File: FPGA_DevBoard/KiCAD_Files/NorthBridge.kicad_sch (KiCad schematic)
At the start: 11 parts, among them J1 4677, J2 DM3D-SF, U1 W25Q128JVSIQ TR, U14 ESP32-WROOM-32UE-N8

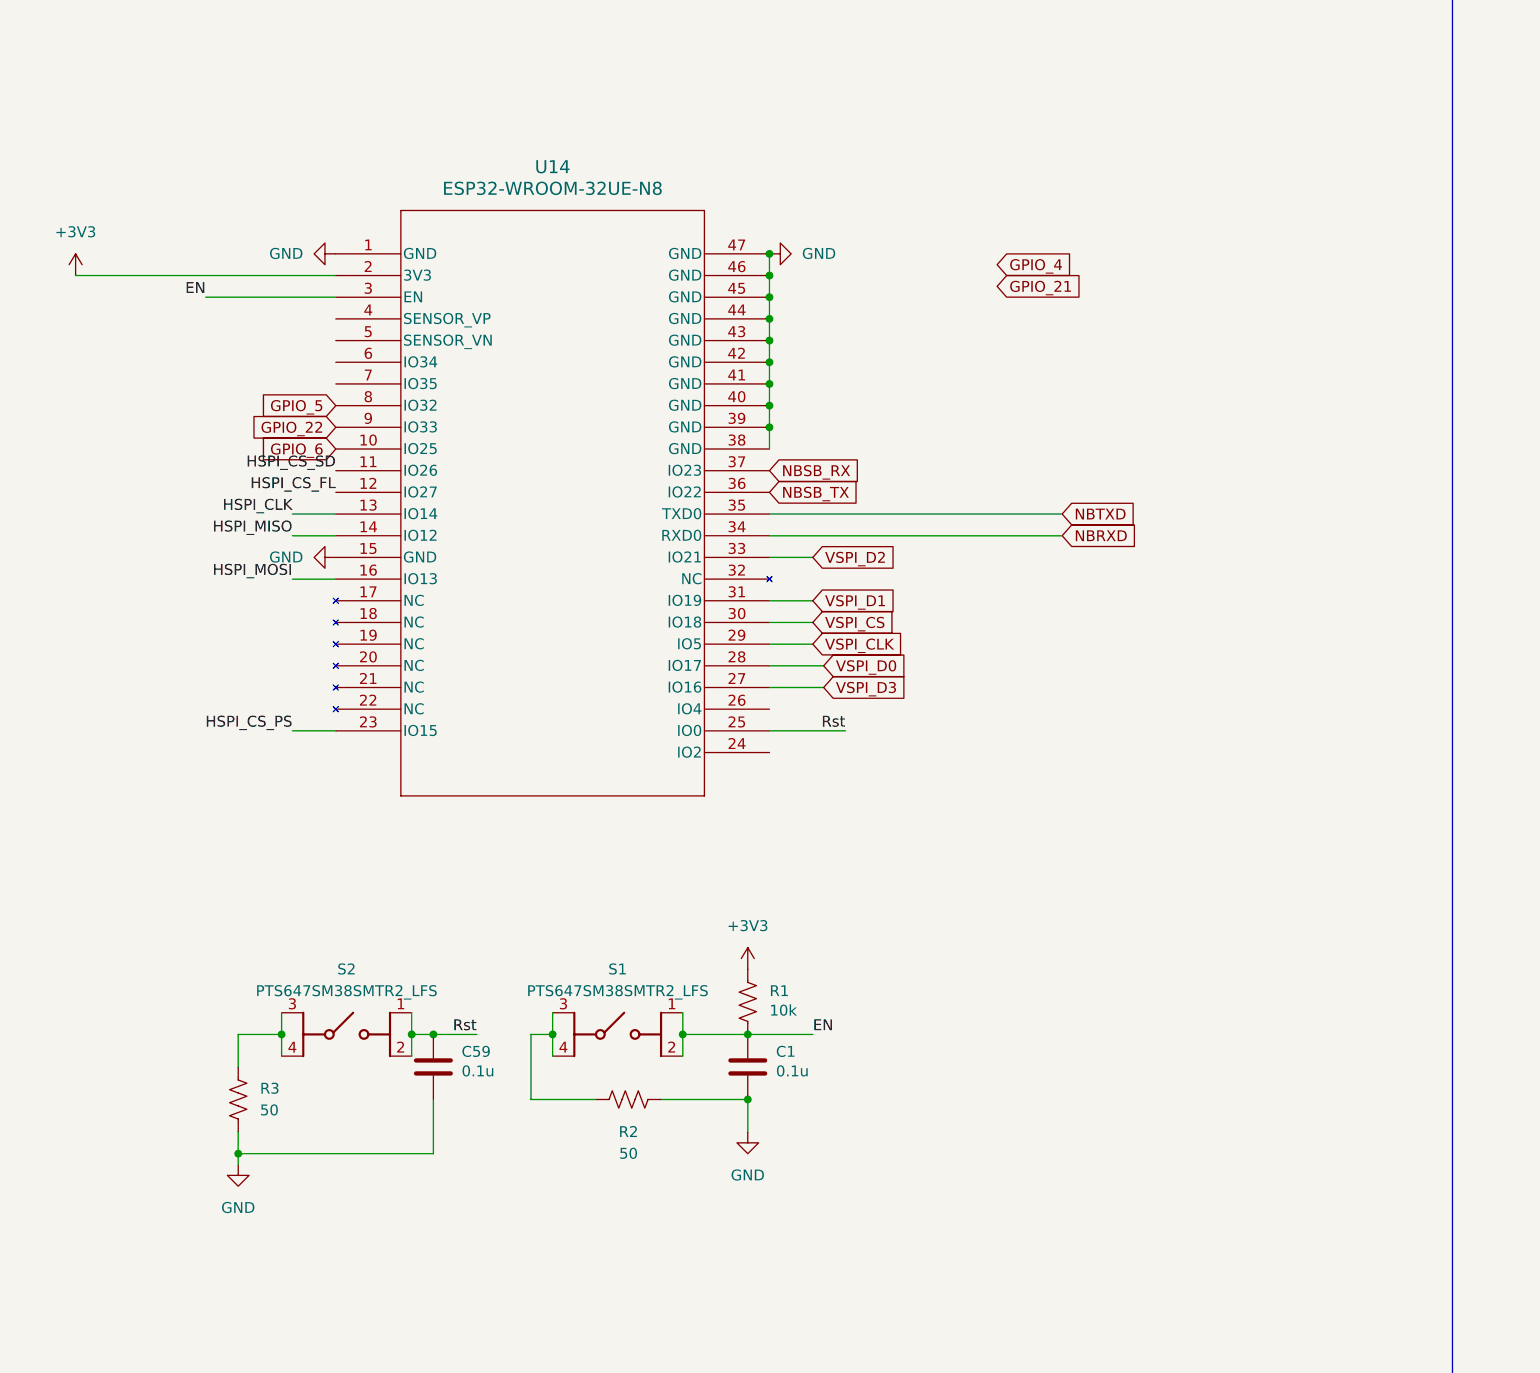
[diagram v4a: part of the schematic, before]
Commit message: OK I PULL UP
Added pull up resistors to SPI CS, pull down to GPIO12, redid vga bus lines. This also might include the FPGA clock being correct? Idk if that was committed before
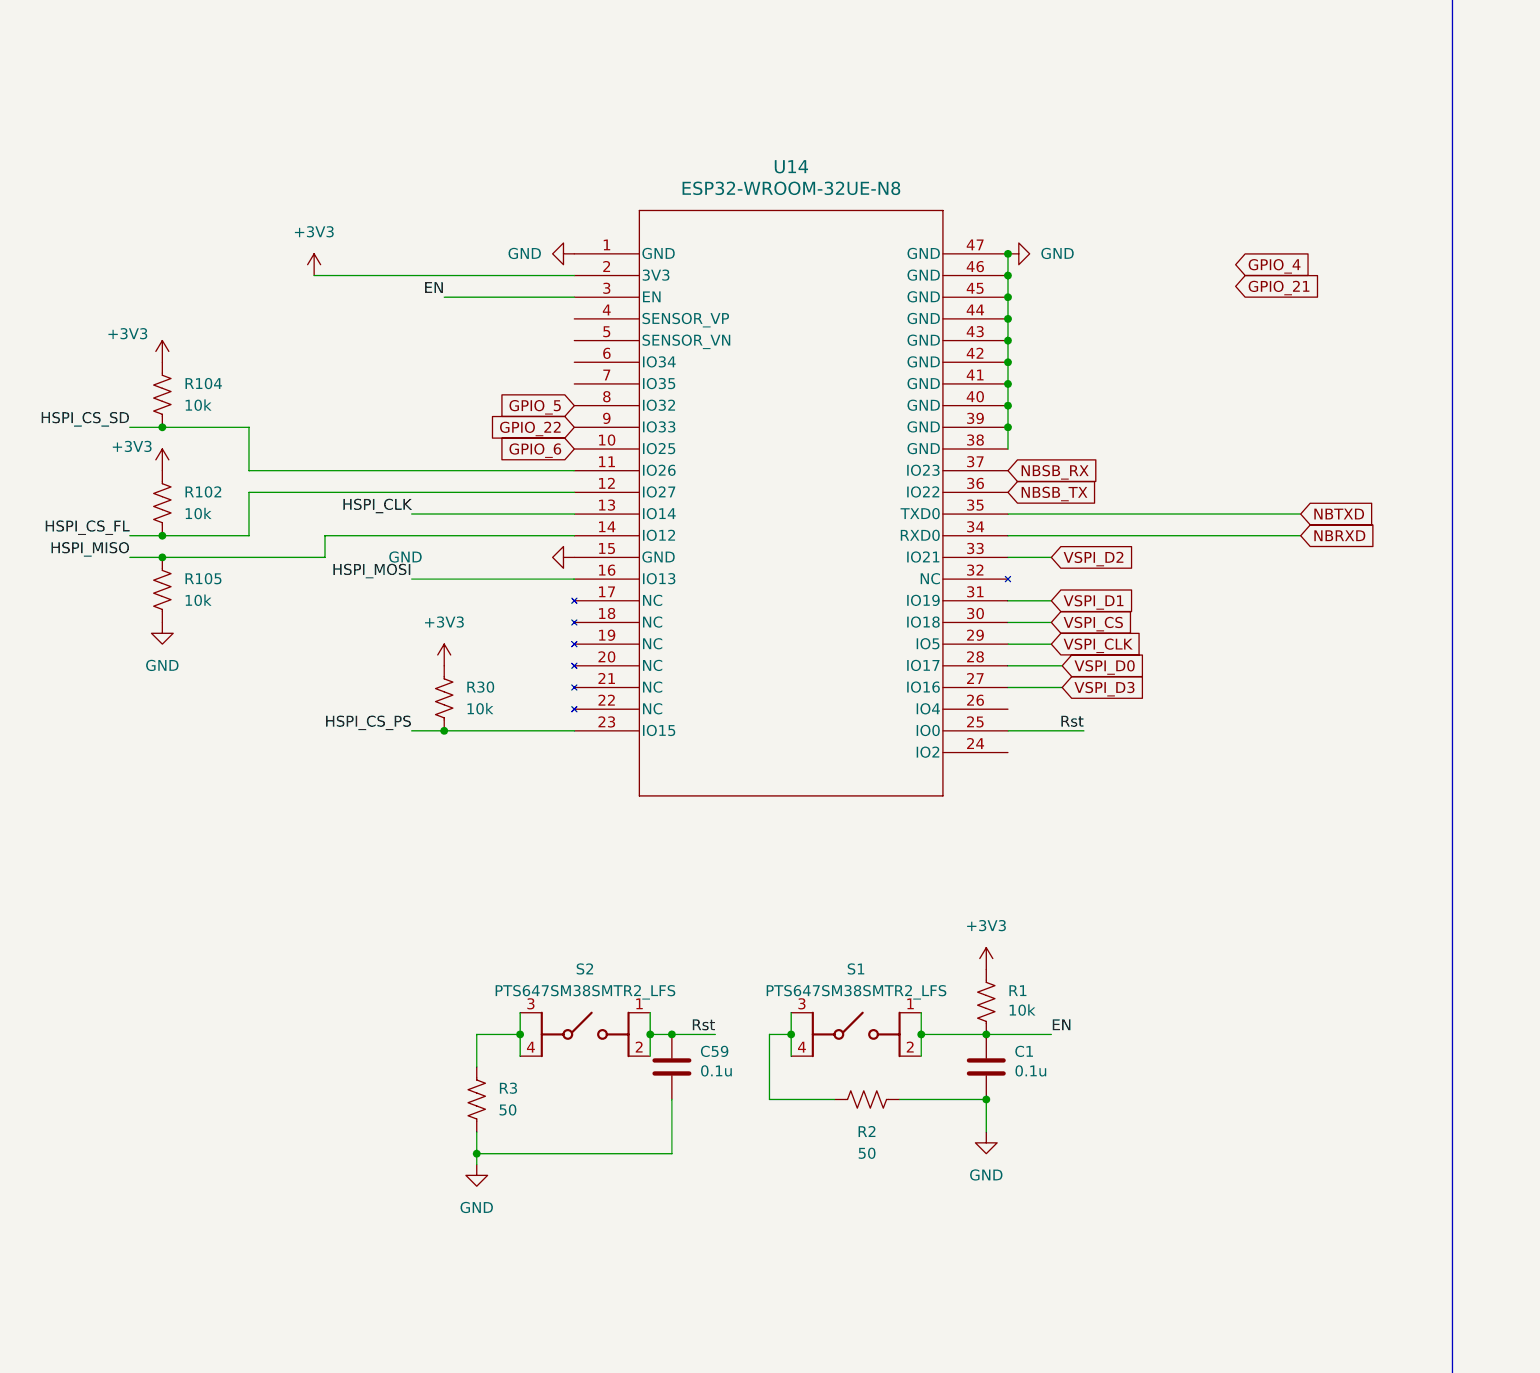
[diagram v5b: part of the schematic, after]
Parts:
- added R102, R104, R105, R30: 10k, Resistor_SMD:R_0402_1005Metric, symbol Device:R_US
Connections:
- net +3V3: now also R102.1, R104.1, R30.1
- net GND: now also R105.2
- net HSPI_CS_FL: now also R102.2
- net HSPI_CS_PS: now also R30.2
- net HSPI_CS_SD: now also R104.2
- net HSPI_MISO: now also R105.1
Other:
- moved on the sheet: C1, C59, R1, R2, R3, S1, S2, U14

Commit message: VGA LENGTH MATCH, LED
Length matched the VGA, updated the GPIO to use the usb host gpio, added some leds and fixed the silkscreen more
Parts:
- added D5: LED, Diode_SMD:D_0603_1608Metric, symbol Device:LED
- added R109: 1k, Resistor_SMD:R_0603_1608Metric, symbol Device:R_US
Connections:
- net EN: now also R109.1
- net GND: now also D5.1 (K)
- new net: D5.2 (A), R109.2

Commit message: Final Final Final Lol
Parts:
- removed R105: 10k, Resistor_SMD:R_0402_1005Metric, symbol Device:R_US
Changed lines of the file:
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@@
-	)
-	(junction
-		(at 27.94 97.79)
-		(diameter 0)
-		(color 0 0 0 0)
 	)
 	(junction
@@
 	(wire
 		(pts
-			(xy 27.94 97.79) (xy 46.99 97.79)
+			(xy 24.13 97.79) (xy 46.99 97.79)
 		)
 		(stroke
@@
 		(pts
 			(xy 57.15 118.11) (xy 60.96 118.11)
-		)
-		(stroke
-			(width 0)
-			(type default)
-		)
-	)
-	(wire
-		(pts
-			(xy 24.13 97.79) (xy 27.94 97.79)
 		)
 		(stroke
@@
 	)
 	(symbol
-		(lib_id "power:GND")
-		(at 27.94 105.41 0)
-		(unit 1)
-		(body_style 1)
-		(exclude_from_sim no)
-		(in_bom yes)
-		(on_board yes)
-		(in_pos_files yes)
-		(dnp no)
-		(fields_autoplaced yes)
-		(property "Reference" "#PWR0113"
-			(at 27.94 111.76 0)
-			(hide yes)
-			(show_name no)
-			(do_not_autoplace no)
-			(effects
-				(font
-					(size 1.27 1.27)
-				)
-			)
-		)
-		(property "Value" "GND"
-			(at 27.94 110.49 0)
-			(show_name no)
-			(do_not_autoplace no)
-			(effects
-				(font
-					(size 1.27 1.27)
-				)
-			)
-		)
-		(property "Footprint" ""
-			(at 27.94 105.41 0)
-			(hide yes)
-			(show_name no)
-			(do_not_autoplace no)
-			(effects
-				(font
-					(size 1.27 1.27)
-				)
-			)
-		)
-		(property "Datasheet" ""
-			(at 27.94 105.41 0)
-			(hide yes)
-			(show_name no)
-			(do_not_autoplace no)
-			(effects
-				(font
-					(size 1.27 1.27)
-				)
-			)
-		)
-		(property "Description" "Power symbol creates a global label with name \"GND\" , ground"
-			(at 27.94 105.41 0)
-			(hide yes)
-			(show_name no)
-			(do_not_autoplace no)
-			(effects
-				(font
-					(size 1.27 1.27)
-				)
-			)
-		)
-		(pin "1"
-		)
-		(instances
-			(project "FPGA_DevBoard"
-				(path "/29dacc10-fb0d-42da-8b4b-fe903faf3f1a/3a4f201e-91d1-46c6-b180-b9c29ee81c31"
-					(reference "#PWR0113")
-					(unit 1)
-				)
-			)
-		)
-	)
-	(symbol
 		(lib_id "power:+3V3")
 		(at 45.72 64.77 0)
@@
 					(unit 1)
 				)
-			)
-		)
-	)
-	(symbol
-		(lib_id "Device:R_US")
-		(at 27.94 101.6 0)
-		(unit 1)
-		(body_style 1)
-		(exclude_from_sim no)
-		(in_bom yes)
-		(on_board yes)
-		(in_pos_files yes)
-		(dnp no)
-		(fields_autoplaced yes)
-		(property "Reference" "R105"
-			(at 30.48 100.3299 0)
-			(show_name no)
-			(do_not_autoplace no)
-			(effects
-				(font
-					(size 1.27 1.27)
-				)
-				(justify left)
-			)
-		)
-		(property "Value" "10k"
-			(at 30.48 102.8699 0)
-			(show_name no)
-			(do_not_autoplace no)
-			(effects
-				(font
-					(size 1.27 1.27)
-				)
-				(justify left)
-			)
-		)
-		(property "Footprint" "Resistor_SMD:R_0402_1005Metric"
-			(at 28.956 101.854 90)
-			(hide yes)
-			(show_name no)
-			(do_not_autoplace no)
-			(effects
-				(font
-					(size 1.27 1.27)
-				)
-			)
-		)
-		(property "Datasheet" ""
-			(at 27.94 101.6 0)
-			(hide yes)
-			(show_name no)
-			(do_not_autoplace no)
-			(effects
-				(font
-					(size 1.27 1.27)
-				)
-			)
-		)
-		(property "Description" "Resistor, US symbol"
-			(at 27.94 101.6 0)
-			(hide yes)
-			(show_name no)
-			(do_not_autoplace no)
-			(effects
-				(font
-					(size 1.27 1.27)
-				)
-			)
-		)
-		(pin "1"
-		)
-		(pin "2"
-		)
-		(instances
-			(project "FPGA_DevBoard"
-				(path "/29dacc10-fb0d-42da-8b4b-fe903faf3f1a/3a4f201e-91d1-46c6-b180-b9c29ee81c31"
-					(reference "R105")
-					(unit 1)
-				)

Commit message: This is V2 Ordered
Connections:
- no-connect marks 12 -> 14
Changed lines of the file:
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@@
+	)
+	(no_connect
+		(at 76.2 69.85)
 	)
 	(no_connect
@@
 	(no_connect
 		(at 318.77 55.88)
+	)
+	(no_connect
+		(at 76.2 72.39)
 	)
 	(no_connect
@@
 		)
 	)
-	(global_label "GPIO_21"
-		(shape input)
-		(at 153.67 66.04 0)
+	(global_label "NBSB_RX"
+		(shape input)
+		(at 127 87.63 0)
 		(fields_autoplaced yes)
 		(effects
@@
 		)
 		(property "Intersheetrefs" "${INTERSHEET_REFS}"
-			(at 164.5171 66.04 0)
+			(at 138.5123 87.63 0)
 			(hide yes)
 			(show_name no)
@@
 		)
 	)
-	(global_label "NBSB_RX"
-		(shape input)
-		(at 127 87.63 0)
+	(global_label "GPIO_5"
+		(shape input)
+		(at 76.2 80.01 180)
+		(fields_autoplaced yes)
+		(effects
+			(font
+				(size 1.27 1.27)
+			)
+			(justify right)
+		)
+		(property "Intersheetrefs" "${INTERSHEET_REFS}"
+			(at 66.5624 80.01 0)
+			(hide yes)
+			(show_name no)
+			(do_not_autoplace no)
+			(effects
+				(font
+					(size 1.27 1.27)
+				)
+				(justify right)
+			)
+		)
+	)
+	(global_label "GPIO_6"
+		(shape input)
+		(at 76.2 85.09 180)
+		(fields_autoplaced yes)
+		(effects
+			(font
+				(size 1.27 1.27)
+			)
+			(justify right)
+		)
+		(property "Intersheetrefs" "${INTERSHEET_REFS}"
+			(at 66.5624 85.09 0)
+			(hide yes)
+			(show_name no)
+			(do_not_autoplace no)
+			(effects
+				(font
+					(size 1.27 1.27)
+				)
+				(justify right)
+			)
+		)
+	)
+	(global_label "VSPI_CS"
+		(shape input)
+		(at 132.08 105.41 0)
 		(fields_autoplaced yes)
 		(effects
@@
 		)
 		(property "Intersheetrefs" "${INTERSHEET_REFS}"
-			(at 138.5123 87.63 0)
+			(at 142.6852 105.41 0)
 			(hide yes)
 			(show_name no)
@@
 		)
 	)
-	(global_label "GPIO_5"
-		(shape input)
-		(at 76.2 80.01 180)
+	(global_label "VSPI_D0"
+		(shape input)
+		(at 133.35 110.49 0)
+		(fields_autoplaced yes)
+		(effects
+			(font
+				(size 1.27 1.27)
+			)
+			(justify left)
+		)
+		(property "Intersheetrefs" "${INTERSHEET_REFS}"
+			(at 143.9552 110.49 0)
+			(hide yes)
+			(show_name no)
+			(do_not_autoplace no)
+			(effects
+				(font
+					(size 1.27 1.27)
+				)
+				(justify left)
+			)
+		)
+	)
+	(global_label "NBTXD"
+		(shape input)
+		(at 161.29 92.71 0)
+		(fields_autoplaced yes)
+		(effects
+			(font
+				(size 1.27 1.27)
+			)
+			(justify left)
+		)
+		(property "Intersheetrefs" "${INTERSHEET_REFS}"
+			(at 170.3228 92.71 0)
+			(hide yes)
+			(show_name no)
+			(do_not_autoplace no)
+			(effects
+				(font
+					(size 1.27 1.27)
+				)
+				(justify left)
+			)
+		)
+	)
+	(global_label "VSPI_D3"
+		(shape input)
+		(at 133.35 113.03 0)
+		(fields_autoplaced yes)
+		(effects
+			(font
+				(size 1.27 1.27)
+			)
+			(justify left)
+		)
+		(property "Intersheetrefs" "${INTERSHEET_REFS}"
+			(at 143.9552 113.03 0)
+			(hide yes)
+			(show_name no)
+			(do_not_autoplace no)
+			(effects
+				(font
+					(size 1.27 1.27)
+				)
+				(justify left)
+			)
+		)
+	)
+	(global_label "VSPI_D1"
+		(shape input)
+		(at 132.08 102.87 0)
+		(fields_autoplaced yes)
+		(effects
+			(font
+				(size 1.27 1.27)
+			)
+			(justify left)
+		)
+		(property "Intersheetrefs" "${INTERSHEET_REFS}"
+			(at 142.6852 102.87 0)
+			(hide yes)
+			(show_name no)
+			(do_not_autoplace no)
+			(effects
+				(font
+					(size 1.27 1.27)
+				)
+				(justify left)
+			)
+		)
+	)
+	(global_label "VSPI_CLK"
+		(shape input)
+		(at 132.08 107.95 0)
+		(fields_autoplaced yes)
+		(effects
+			(font
+				(size 1.27 1.27)
+			)
+			(justify left)
+		)
+		(property "Intersheetrefs" "${INTERSHEET_REFS}"
+			(at 143.7738 107.95 0)
+			(hide yes)
+			(show_name no)
+			(do_not_autoplace no)
+			(effects
+				(font
+					(size 1.27 1.27)
+				)
+				(justify left)
+			)
+		)
+	)
+	(global_label "GPIO_22"
+		(shape input)
+		(at 76.2 82.55 180)
 		(fields_autoplaced yes)
 		(effects
@@
 		)
 		(property "Intersheetrefs" "${INTERSHEET_REFS}"
-			(at 66.5624 80.01 0)
+			(at 65.3529 82.55 0)
 			(hide yes)
 			(show_name no)
@@
 		)
 	)
-	(global_label "GPIO_6"
-		(shape input)
-		(at 76.2 85.09 180)
-		(fields_autoplaced yes)
-		(effects
-			(font
-				(size 1.27 1.27)
-			)
-			(justify right)
-		)
-		(property "Intersheetrefs" "${INTERSHEET_REFS}"
-			(at 66.5624 85.09 0)
-			(hide yes)
-			(show_name no)
-			(do_not_autoplace no)
-			(effects
-				(font
-					(size 1.27 1.27)
-				)
-				(justify right)
-			)
-		)
-	)
-	(global_label "VSPI_CS"
-		(shape input)
-		(at 132.08 105.41 0)
+	(global_label "NBRXD"
+		(shape input)
+		(at 161.29 95.25 0)
 		(fields_autoplaced yes)
 		(effects
@@
 		)
 		(property "Intersheetrefs" "${INTERSHEET_REFS}"
-			(at 142.6852 105.41 0)
-			(hide yes)
-			(show_name no)
-			(do_not_autoplace no)
-			(effects
-				(font
-					(size 1.27 1.27)
-				)
-				(justify left)
-			)
-		)
-	)
-	(global_label "VSPI_D0"
-		(shape input)
-		(at 133.35 110.49 0)
-		(fields_autoplaced yes)
-		(effects
-			(font
-				(size 1.27 1.27)
-			)
-			(justify left)
-		)
-		(property "Intersheetrefs" "${INTERSHEET_REFS}"
-			(at 143.9552 110.49 0)
-			(hide yes)
-			(show_name no)
-			(do_not_autoplace no)
-			(effects
-				(font
-					(size 1.27 1.27)
-				)
-				(justify left)
-			)
-		)
-	)
-	(global_label "NBTXD"
-		(shape input)
-		(at 161.29 92.71 0)
-		(fields_autoplaced yes)
-		(effects
-			(font
-				(size 1.27 1.27)
-			)
-			(justify left)
-		)
-		(property "Intersheetrefs" "${INTERSHEET_REFS}"
-			(at 170.3228 92.71 0)
-			(hide yes)
-			(show_name no)
-			(do_not_autoplace no)
-			(effects
-				(font
-					(size 1.27 1.27)
-				)
-				(justify left)
-			)
-		)
-	)
-	(global_label "VSPI_D3"
-		(shape input)
-		(at 133.35 113.03 0)
-		(fields_autoplaced yes)
-		(effects
-			(font
-				(size 1.27 1.27)
-			)
-			(justify left)
-		)
-		(property "Intersheetrefs" "${INTERSHEET_REFS}"
-			(at 143.9552 113.03 0)
-			(hide yes)
-			(show_name no)
-			(do_not_autoplace no)
-			(effects
-				(font
-					(size 1.27 1.27)
-				)
-				(justify left)
-			)
-		)
-	)
-	(global_label "VSPI_D1"
-		(shape input)
-		(at 132.08 102.87 0)
-		(fields_autoplaced yes)
-		(effects
-			(font
-				(size 1.27 1.27)
-			)
-			(justify left)
-		)
-		(property "Intersheetrefs" "${INTERSHEET_REFS}"
-			(at 142.6852 102.87 0)
-			(hide yes)
-			(show_name no)
-			(do_not_autoplace no)
-			(effects
-				(font
-					(size 1.27 1.27)
-				)
-				(justify left)
-			)
-		)
-	)
-	(global_label "VSPI_CLK"
-		(shape input)
-		(at 132.08 107.95 0)
-		(fields_autoplaced yes)
-		(effects
-			(font
-				(size 1.27 1.27)
-			)
-			(justify left)
-		)
-		(property "Intersheetrefs" "${INTERSHEET_REFS}"
-			(at 143.7738 107.95 0)
-			(hide yes)
-			(show_name no)
-			(do_not_autoplace no)
-			(effects
-				(font
-					(size 1.27 1.27)
-				)
-				(justify left)
-			)
-		)
-	)
-	(global_label "GPIO_22"
-		(shape input)
-		(at 76.2 82.55 180)
-		(fields_autoplaced yes)
-		(effects
-			(font
-				(size 1.27 1.27)
-			)
-			(justify right)
-		)
-		(property "Intersheetrefs" "${INTERSHEET_REFS}"
-			(at 65.3529 82.55 0)
-			(hide yes)
-			(show_name no)
-			(do_not_autoplace no)
-			(effects
-				(font
-					(size 1.27 1.27)
-				)
-				(justify right)
-			)
-		)
-	)
-	(global_label "NBRXD"
-		(shape input)
-		(at 161.29 95.25 0)
-		(fields_autoplaced yes)
-		(effects
-			(font
-				(size 1.27 1.27)
-			)
-			(justify left)
-		)
-		(property "Intersheetrefs" "${INTERSHEET_REFS}"
 			(at 170.6252 95.25 0)
 			(hide yes)
 			(show_name no)
-			(do_not_autoplace no)
-			(effects
-				(font
-					(size 1.27 1.27)
-				)
-				(justify left)
-			)
-		)
-	)
-	(global_label "GPIO_4"
-		(shape input)
-		(at 153.67 63.5 0)
-		(fields_autoplaced yes)
-		(effects
-			(font
-				(size 1.27 1.27)
-			)
-			(justify left)
-		)
-		(property "Intersheetrefs" "${INTERSHEET_REFS}"
-			(at 163.3076 63.5 0)
-			(hide yes)
-			(show_name no)
